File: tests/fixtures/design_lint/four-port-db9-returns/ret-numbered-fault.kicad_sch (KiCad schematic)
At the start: 4 parts, among them J1 Synthetic DB9 connector, J2 Synthetic DB9 connector, J3 Synthetic DB9 connector, J4 Synthetic DB9 connector

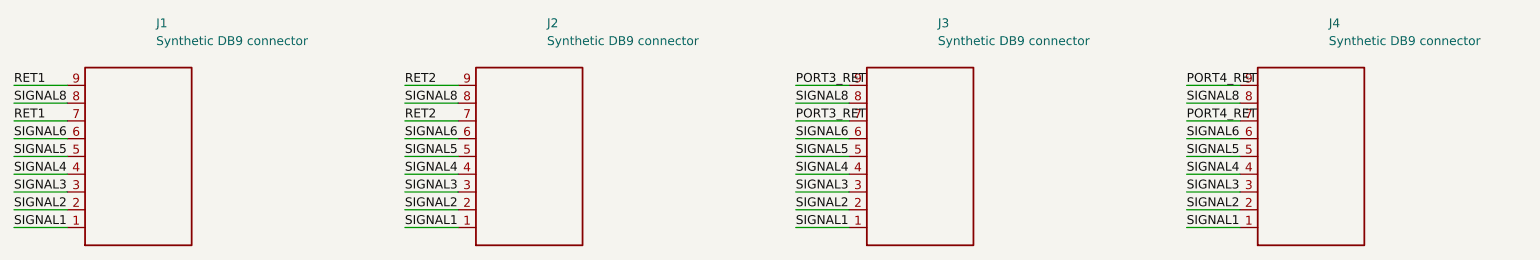
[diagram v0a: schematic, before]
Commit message: feat: review compact protocol return groups
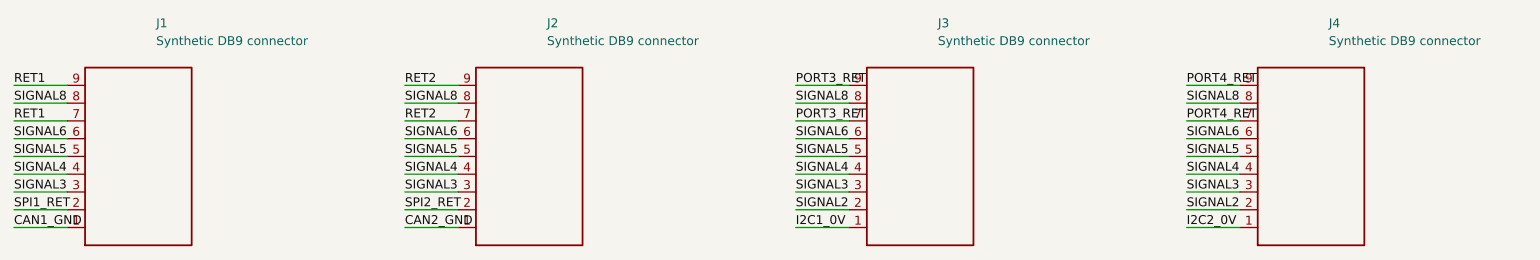
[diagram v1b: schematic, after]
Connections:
- net SIGNAL2: no longer J1.2 (SIGNAL2), J2.2 (SIGNAL2)
- removed net SIGNAL1: J1.1 (SIGNAL1), J2.1 (SIGNAL1), J3.1 (SIGNAL1), J4.1 (SIGNAL1)
- new net CAN1_GND: J1.1 (GND)
- new net CAN2_GND: J2.1 (GND)
- new net I2C1_0V: J3.1 (GND)
- new net I2C2_0V: J4.1 (GND)
- new net SPI1_RET: J1.2 (GND)
- new net SPI2_RET: J2.2 (GND)
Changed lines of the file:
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@@
     (stroke (width 0) (type default))
 )
-  (label "SIGNAL1" (at 43.18 111.76 0)
+  (label "CAN1_GND" (at 43.18 111.76 0)
     (effects (font (size 1.27 1.27)) (justify left bottom))
 )
@@
     (stroke (width 0) (type default))
 )
-  (label "SIGNAL2" (at 43.18 109.22 0)
+  (label "SPI1_RET" (at 43.18 109.22 0)
     (effects (font (size 1.27 1.27)) (justify left bottom))
 )
@@
     (stroke (width 0) (type default))
 )
-  (label "SIGNAL1" (at 99.06 111.76 0)
+  (label "CAN2_GND" (at 99.06 111.76 0)
     (effects (font (size 1.27 1.27)) (justify left bottom))
 )
@@
     (stroke (width 0) (type default))
 )
-  (label "SIGNAL2" (at 99.06 109.22 0)
+  (label "SPI2_RET" (at 99.06 109.22 0)
     (effects (font (size 1.27 1.27)) (justify left bottom))
 )
@@
     (stroke (width 0) (type default))
 )
-  (label "SIGNAL1" (at 154.94 111.76 0)
+  (label "I2C1_0V" (at 154.94 111.76 0)
     (effects (font (size 1.27 1.27)) (justify left bottom))
 )
@@
     (stroke (width 0) (type default))
 )
-  (label "SIGNAL1" (at 210.82 111.76 0)
+  (label "I2C2_0V" (at 210.82 111.76 0)
     (effects (font (size 1.27 1.27)) (justify left bottom))
 )
